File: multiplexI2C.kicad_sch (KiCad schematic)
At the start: 23 parts, among them J17 Conn_01x04_Pin, J18 PinSocket_1x20_P2.54mm_Vertic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, J19 PinSocket_1x20_P2.54mm_Vertic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, J20 Screw_Terminal_01x02, SW1 SW_DIP_x03, U1 PCA9548ADW

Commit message: clean up symbol fields
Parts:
- C5, C6, C7, C8, C9, R1, R2, R23, R25, R3, R4: MountType (none) -> SMT
- H1, H2, H3, H4, J**1, J**2: MountType (none) -> PTH
- J17: Manufacturer (none) -> JST; MfgPart (none) -> XH_B4B-XH-A; MountType (none) -> PTH; Notes (none) -> or equivalent
- J18, J19: Manufacturer (none) -> JILN; MfgPart (none) -> 22850120ANG1SYA01; MountType (none) -> PTH; Notes (none) -> or equivalent
- J20: Manufacturer (none) -> Cixi Kefa Elec; MfgPart (none) -> KF128-2.54-2P; MountType (none) -> PTH; Notes (none) -> or equivalent
- SW1: Manufacturer (none) -> King Tek; MfgPart (none) -> DSHP03TS ??; MountType (none) -> SMT; Notes (none) -> or equivalent
- U1: MfgPart (none) -> PCA9548ADW; MountType (none) -> SMT; Notes (none) -> or equivalent

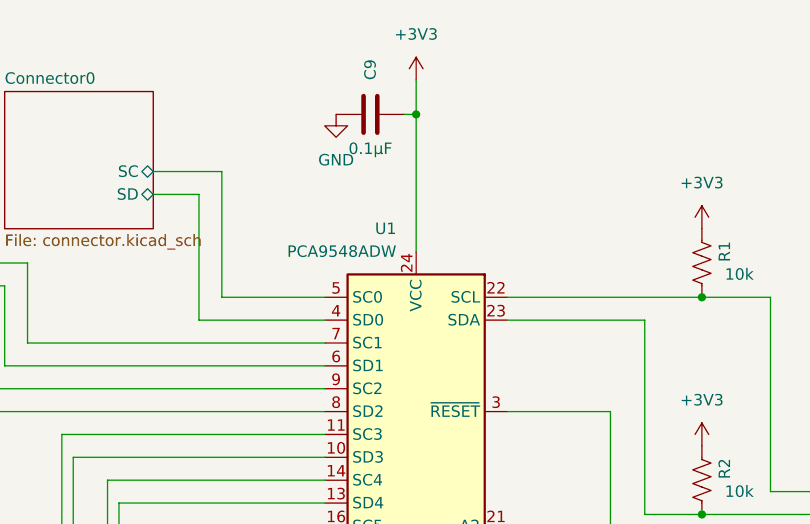
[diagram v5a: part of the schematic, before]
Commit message: passing checks with TCA9548A in pass. Ongoingg cleanup.
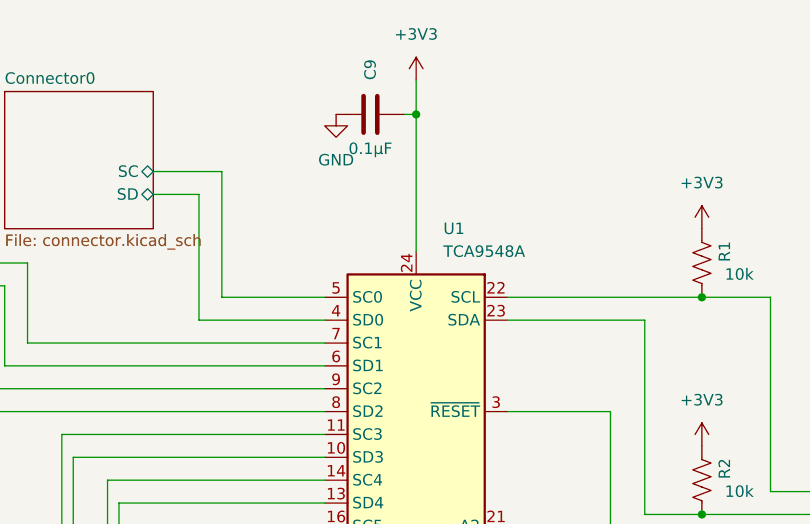
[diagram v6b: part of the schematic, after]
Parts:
- U1: value PCA9548ADW -> TCA9548A; footprint Package_SO:SOIC-24W_7.5x15.4mm_P1.27mm -> Package_SO:TSSOP-24_4.4x7.8mm_P0.65mm; symbol ProjectLib:PCA9548ADW -> ProjectLib:TCA9548APWR
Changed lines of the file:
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@@
 	)
 	(symbol
-		(lib_id "ProjectLib:PCA9548ADW")
+		(lib_id "ProjectLib:TCA9548APWR")
 		(at 104.14 63.5 0)
 		(mirror y)
@@
 		(fields_autoplaced yes)
 		(property "Reference" "U1"
-			(at 101.9459 38.1 0)
+			(at 107.1565 38.1 0)
 			(effects
 				(font
 					(size 1.27 1.27)
 				)
-				(justify left)
+				(justify right)
 			)
 		)
-		(property "Value" "PCA9548ADW"
-			(at 101.9459 40.64 0)
+		(property "Value" "TCA9548A"
+			(at 107.1565 40.64 0)
 			(effects
 				(font
 					(size 1.27 1.27)
 				)
-				(justify left)
+				(justify right)
 			)
 		)
-		(property "Footprint" "Package_SO:SOIC-24W_7.5x15.4mm_P1.27mm"
+		(property "Footprint" "Package_SO:TSSOP-24_4.4x7.8mm_P0.65mm"
 			(at 104.14 88.9 0)
 			(effects
@@
 			)
 		)
-		(property "Datasheet" "http://www.ti.com/lit/ds/symlink/pca9548a.pdf"
+		(property "Datasheet" "http://www.ti.com/lit/ds/symlink/tca9548a.pdf"
 			(at 102.87 57.15 0)
 			(effects
@@
 			)
 		)
-		(property "Description" "Low voltage 8-channel I2C switch with reset, SOIC-24"
+		(property "Description" "Low voltage 8-channel I2C switch with reset, TSSOP-24"
 			(at 104.14 63.5 0)
 			(effects

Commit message: added TCA footprint to ProjectLib. Minor cleanup and fiddling with README graphics.
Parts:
- U1: footprint Package_SO:TSSOP-24_4.4x7.8mm_P0.65mm -> ProjectLib:TSSOP-24_4.4x7.8mm_P0.65mm; Manufacturer (none) -> TI; MfgPart PCA9548ADW -> TCA9548A
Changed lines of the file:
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@@
 			)
 		)
-		(property "Footprint" "Package_SO:TSSOP-24_4.4x7.8mm_P0.65mm"
+		(property "Footprint" "ProjectLib:TSSOP-24_4.4x7.8mm_P0.65mm"
 			(at 104.14 88.9 0)
 			(effects
@@
 			)
 		)
-		(property "Manufacturer" ""
+		(property "Manufacturer" "TI"
 			(at 104.14 63.5 0)
 			(effects
@@
 			)
 		)
-		(property "MfgPart" "PCA9548ADW"
+		(property "MfgPart" "TCA9548A"
 			(at 104.14 63.5 0)
 			(effects

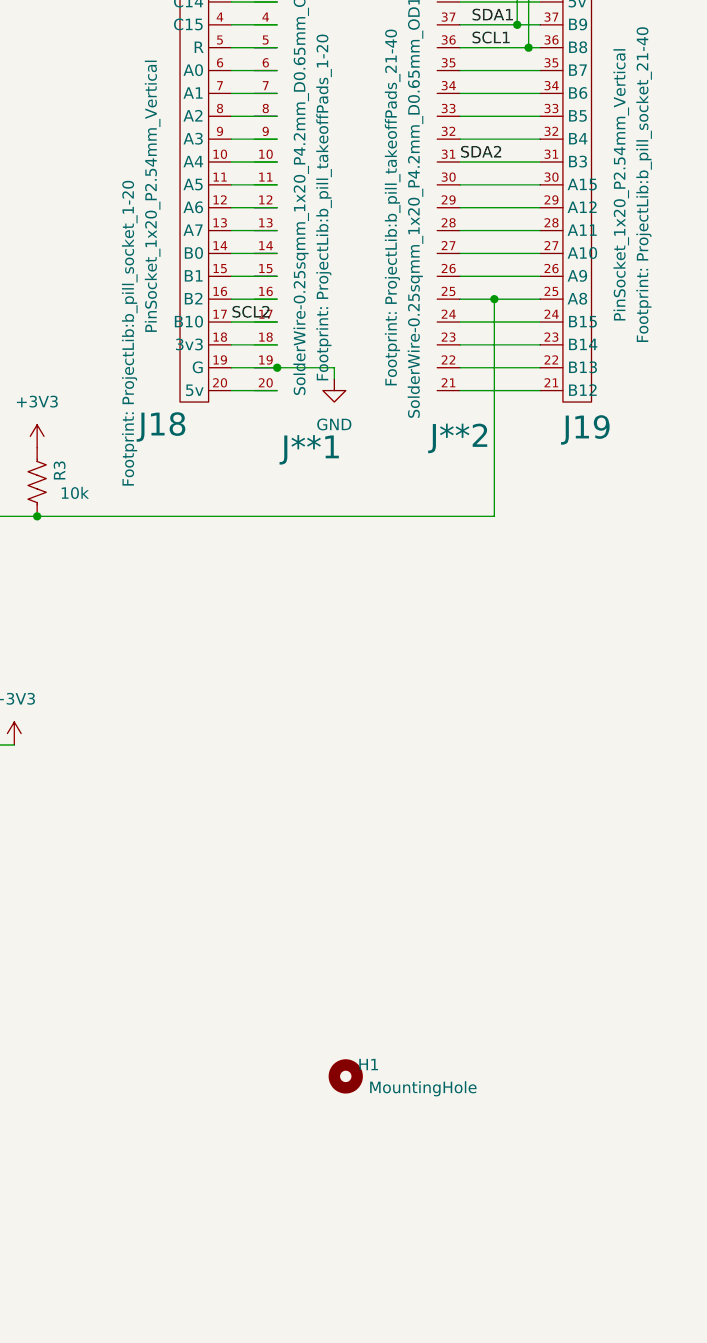
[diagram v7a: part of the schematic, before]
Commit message: added header for ssd1306.
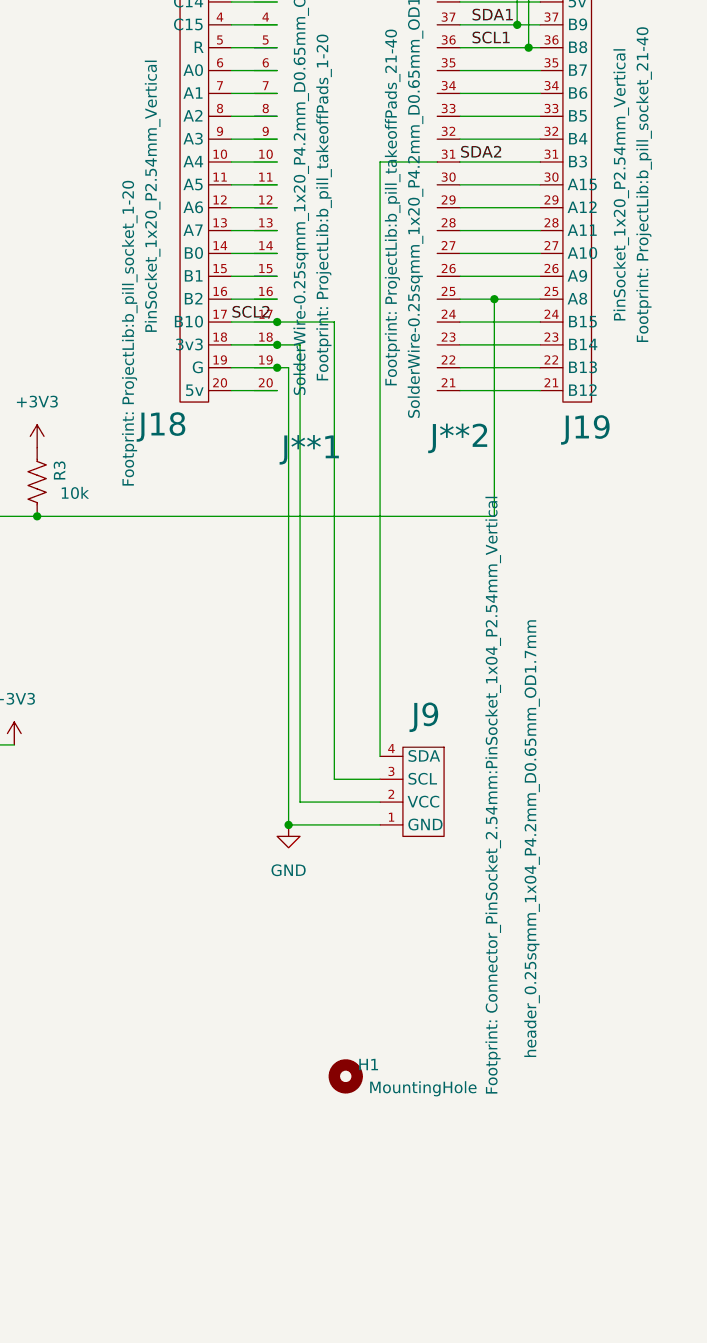
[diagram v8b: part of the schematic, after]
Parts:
- added J9: header_0.25sqmm_1x04_P4.2mm_D0.65mm_OD1.7mm, Connector_PinSocket_2.54mm:PinSocket_1x04_P2.54mm_Vertical, symbol ProjectLib:ssd1306_header
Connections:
- net GND: now also J9.1 (GND)
- net SCL2: now also J9.3 (SCL)
- net at J**1.18, J18.18 (3v3): now also J9.2 (VCC)
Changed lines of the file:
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@@
 	)
 	(junction
+		(at 162.56 146.05)
+		(diameter 0)
+		(color 0 0 0 0)
+	)
+	(junction
+		(at 163.83 199.39)
+		(diameter 0)
+		(color 0 0 0 0)
+	)
+	(junction
 		(at 161.29 86.36)
 		(diameter 0)
@@
 	)
 	(junction
-		(at 167.64 64.77)
+		(at 162.56 143.51)
 		(diameter 0)
 		(color 0 0 0 0)
 	)
 	(junction
-		(at 135.89 165.1)
+		(at 167.64 64.77)
 		(diameter 0)
 		(color 0 0 0 0)
 	)
 	(junction
-		(at 78.74 198.12)
+		(at 135.89 165.1)
 		(diameter 0)
 		(color 0 0 0 0)
 	)
 	(junction
-		(at 186.69 140.97)
+		(at 78.74 198.12)
 		(diameter 0)
 		(color 0 0 0 0)
 	)
 	(junction
-		(at 162.56 148.59)
+		(at 186.69 140.97)
 		(diameter 0)
 		(color 0 0 0 0)
@@
 	)
 	(junction
+		(at 162.56 148.59)
+		(diameter 0)
+		(color 0 0 0 0)
+	)
+	(junction
 		(at 186.69 62.23)
 		(diameter 0)
@@
 	(wire
 		(pts
+			(xy 165.1 196.85) (xy 173.99 196.85)
+		)
+		(stroke
+			(width 0)
+			(type default)
+		)
+	)
+	(wire
+		(pts
 			(xy 176.53 62.23) (xy 186.69 62.23)
 		)
@@
 	(wire
 		(pts
+			(xy 163.83 199.39) (xy 173.99 199.39)
+		)
+		(stroke
+			(width 0)
+			(type default)
+		)
+	)
+	(wire
+		(pts
 			(xy 91.44 163.83) (xy 91.44 81.28)
 		)
@@
 	(wire
 		(pts
-			(xy 168.91 148.59) (xy 168.91 149.86)
+			(xy 163.83 148.59) (xy 163.83 199.39)
 		)
 		(stroke
@@
 	(wire
 		(pts
-			(xy 162.56 148.59) (xy 168.91 148.59)
-		)
-		(stroke
-			(width 0)
-			(type default)
-		)
-	)
-	(wire
-		(pts
 			(xy 64.77 60.96) (xy 93.98 60.96)
 		)
@@
 	(wire
 		(pts
+			(xy 180.34 125.73) (xy 173.99 125.73)
+		)
+		(stroke
+			(width 0)
+			(type default)
+		)
+	)
+	(wire
+		(pts
 			(xy 69.85 66.04) (xy 93.98 66.04)
 		)
@@
 	(wire
 		(pts
+			(xy 162.56 146.05) (xy 165.1 146.05)
+		)
+		(stroke
+			(width 0)
+			(type default)
+		)
+	)
+	(wire
+		(pts
 			(xy 182.88 105.41) (xy 186.69 105.41)
 		)
@@
 	(wire
 		(pts
+			(xy 173.99 125.73) (xy 173.99 191.77)
+		)
+		(stroke
+			(width 0)
+			(type default)
+		)
+	)
+	(wire
+		(pts
 			(xy 157.48 105.41) (xy 162.56 105.41)
 		)
@@
 	(wire
 		(pts
+			(xy 162.56 148.59) (xy 163.83 148.59)
+		)
+		(stroke
+			(width 0)
+			(type default)
+		)
+	)
+	(wire
+		(pts
 			(xy 157.48 135.89) (xy 162.56 135.89)
 		)
@@
 	(wire
 		(pts
+			(xy 168.91 143.51) (xy 168.91 194.31)
+		)
+		(stroke
+			(width 0)
+			(type default)
+		)
+	)
+	(wire
+		(pts
 			(xy 182.88 115.57) (xy 191.77 115.57)
 		)
@@
 	(wire
 		(pts
+			(xy 168.91 194.31) (xy 173.99 194.31)
+		)
+		(stroke
+			(width 0)
+			(type default)
+		)
+	)
+	(wire
+		(pts
 			(xy 49.53 142.24) (xy 86.36 142.24)
 		)
@@
 	(wire
 		(pts
+			(xy 165.1 146.05) (xy 165.1 196.85)
+		)
+		(stroke
+			(width 0)
+			(type default)
+		)
+	)
+	(wire
+		(pts
 			(xy 114.3 58.42) (xy 125.73 58.42)
 		)
@@
 	(wire
 		(pts
+			(xy 162.56 143.51) (xy 168.91 143.51)
+		)
+		(stroke
+			(width 0)
+			(type default)
+		)
+	)
+	(wire
+		(pts
 			(xy 143.51 67.31) (xy 190.5 67.31)
 		)
@@
 	)
 	(symbol
+		(lib_id "ProjectLib:ssd1306_header")
+		(at 176.53 195.58 0)
+		(mirror y)
+		(unit 1)
+		(exclude_from_sim no)
+		(in_bom yes)
+		(on_board yes)
+		(dnp no)
+		(property "Reference" "J9"
+			(at 179.07 187.198 0)
+			(effects
+				(font
+					(size 2.54 2.54)
+				)
+			)
+		)
+		(property "Value" "header_0.25sqmm_1x04_P4.2mm_D0.65mm_OD1.7mm"
+			(at 190.754 200.914 90)
+			(effects
+				(font
+					(size 1.27 1.27)
+				)
+			)
+		)
+		(property "Footprint" "Connector_PinSocket_2.54mm:PinSocket_1x04_P2.54mm_Vertical"
+			(at 186.436 196.088 90)
+			(show_name yes)
+			(effects
+				(font
+					(size 1.27 1.27)
+				)
+			)
+		)
+		(property "Datasheet" ""
+			(at 151.384 197.866 0)
+			(effects
+				(font
+					(size 1.27 1.27)
+				)
+				(hide yes)
+			)
+		)
+		(property "Description" "4P I2C header for SSD1306 module"
+			(at 165.608 201.676 0)
+			(effects
+				(font
+					(size 1.27 1.27)
+				)
+				(hide yes)
+			)
+		)
+		(pin "4"
+		)
+		(pin "3"
+		)
+		(pin "2"
+		)
+		(pin "1"
+		)
+		(instances
+			(project ""
+				(path "/0c2d0c14-8850-4a30-bb78-b2f40cb442ba"
+					(reference "J9")
+					(unit 1)
+				)
+			)
+		)
+	)
+	(symbol
 		(lib_id "ProjectLib:b_pill_takeoff_21-40")
 		(at 167.64 128.27 0)
@@
 	(symbol
 		(lib_id "power:GND")
-		(at 168.91 149.86 0)
+		(at 163.83 199.39 0)
 		(unit 1)
 		(exclude_from_sim no)
@@
 		(fields_autoplaced yes)
 		(property "Reference" "#PWR049"
-			(at 168.91 156.21 0)
+			(at 163.83 205.74 0)
 			(effects
 				(font
@@
 		)
 		(property "Value" "GND"
-			(at 168.91 154.94 0)
+			(at 163.83 204.47 0)
 			(effects
 				(font
@@
 		)
 		(property "Footprint" ""
-			(at 168.91 149.86 0)
+			(at 163.83 199.39 0)
 			(effects
 				(font
@@
 		)
 		(property "Datasheet" ""
-			(at 168.91 149.86 0)
+			(at 163.83 199.39 0)
 			(effects
 				(font
@@
 		)
 		(property "Description" "Power symbol creates a global label with name \"GND\" , ground"
-			(at 168.91 149.86 0)
+			(at 163.83 199.39 0)
 			(effects
 				(font
